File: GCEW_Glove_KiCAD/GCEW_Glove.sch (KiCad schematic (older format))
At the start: 35 parts, among them J1 Conn_02x03_Odd_Even, J2 Flex_Sensor_Inputs, SW1 SW_SPDT, SW2 SW_Push, U1 TLV809-DBV, U2 LM3668, U3 ATMEGA328PB-AU, U4 HC-05_BluetoothModule

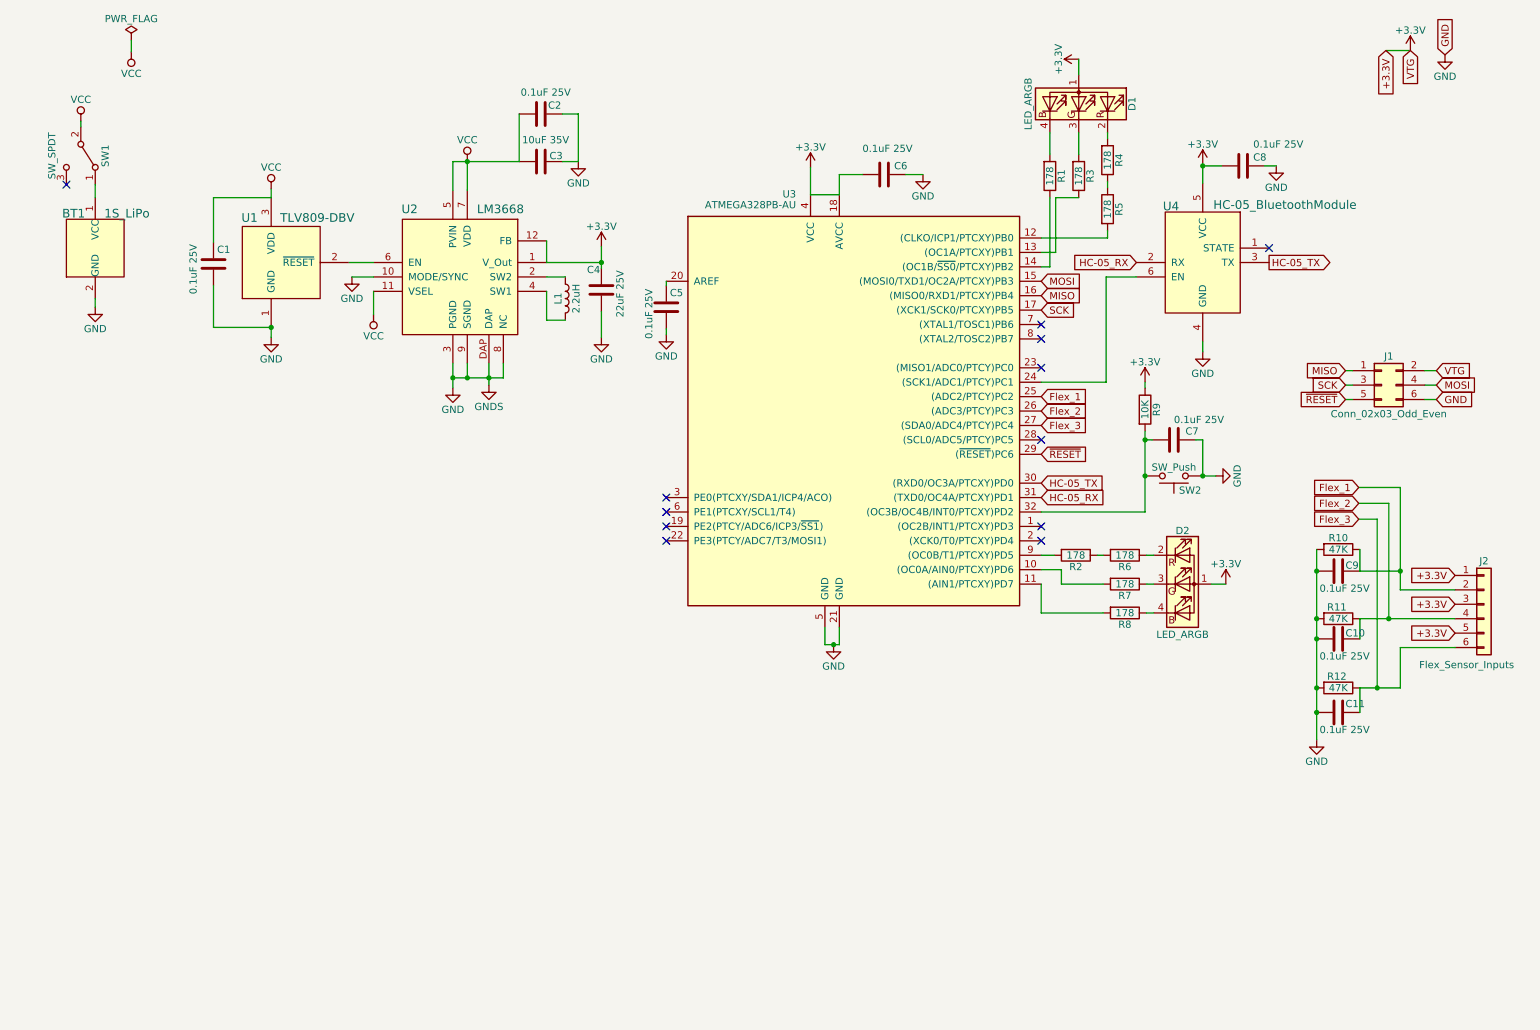
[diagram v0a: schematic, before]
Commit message: GCEW Glove Schematic Update 4
Fixed PCB design error with Bluetooth module. Added additional labels on silkscreen layers.
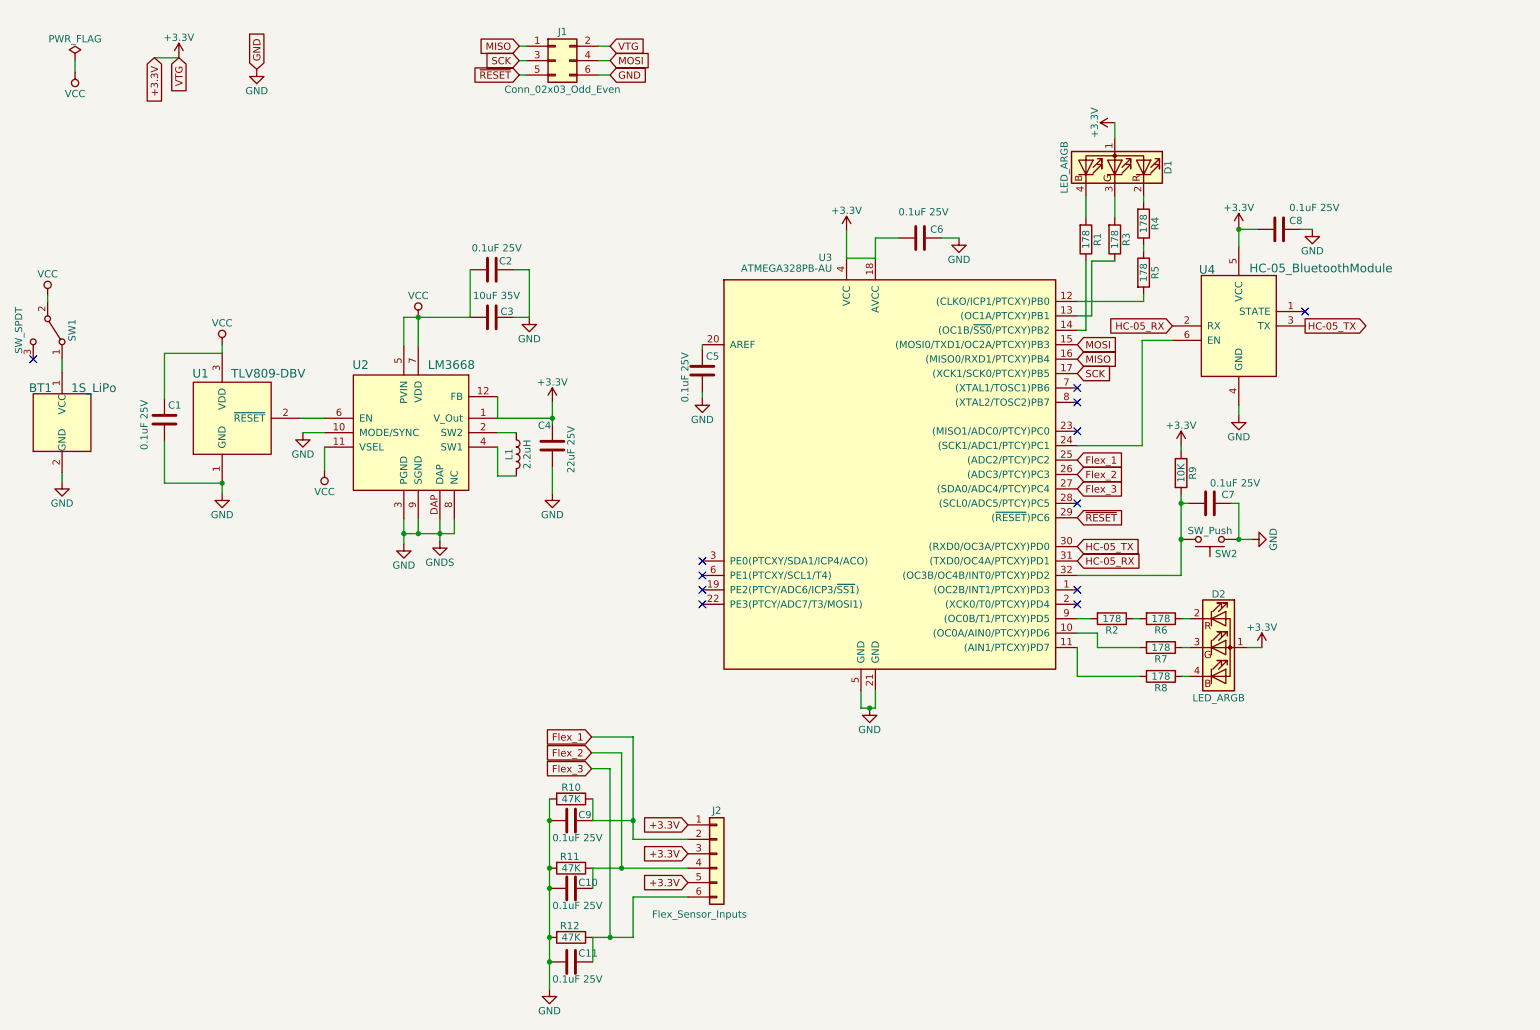
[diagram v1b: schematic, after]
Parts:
- C4: footprint Capacitors_SMD:C_0805_HandSoldering -> Capacitors_SMD:C_0805
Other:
- moved on the sheet: BT1, C1, C10, C11, C2, C3, C4, C5, C6, C7, C8, C9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

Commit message: First Upload
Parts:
- BT1: symbol 1S_LiPo -> GCEW_Glove-rescue:1S_LiPo
- C1, C10, C11, C2, C3, C4, C5, C6, C7, C8, C9: symbol C -> GCEW_Glove-rescue:C
- D1, D2: symbol LED_ARGB -> GCEW_Glove-rescue:LED_ARGB
- J1: symbol Conn_02x03_Odd_Even -> GCEW_Glove-rescue:Conn_02x03_Odd_Even
- J2: symbol Conn_01x06 -> GCEW_Glove-rescue:Conn_01x06
- L1: symbol L -> GCEW_Glove-rescue:L
- R1, R10, R11, R12, R2, R3, R4, R5, R6, R7, R8, R9: symbol R -> GCEW_Glove-rescue:R
- SW1: symbol SW_SPDT -> GCEW_Glove-rescue:SW_SPDT
- SW2: symbol SW_Push -> GCEW_Glove-rescue:SW_Push
- U1: symbol TLV809-DBV -> GCEW_Glove-rescue:TLV809-DBV
- U2: symbol LM3668 -> GCEW_Glove-rescue:LM3668
- U3: symbol ATMEGA328PB-AU -> GCEW_Glove-rescue:ATMEGA328PB-AU
- U4: symbol HC-05_BluetoothModule -> GCEW_Glove-rescue:HC-05_BluetoothModule
